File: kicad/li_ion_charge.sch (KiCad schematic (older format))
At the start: 1 part

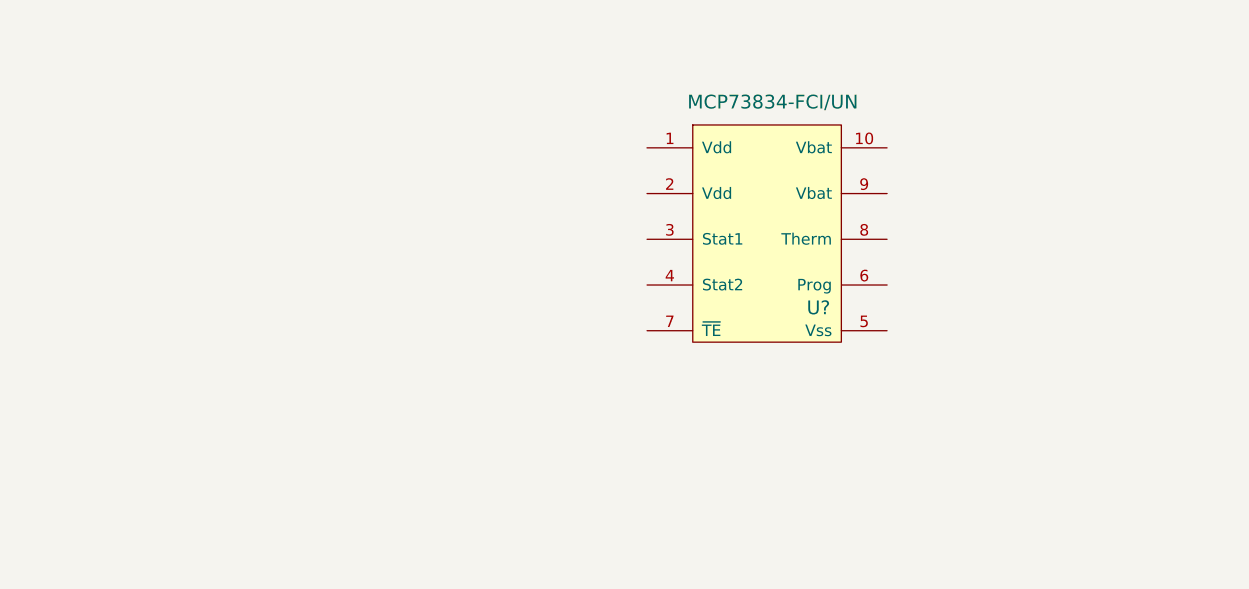
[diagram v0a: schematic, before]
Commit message: Initial implementation of schematic with values
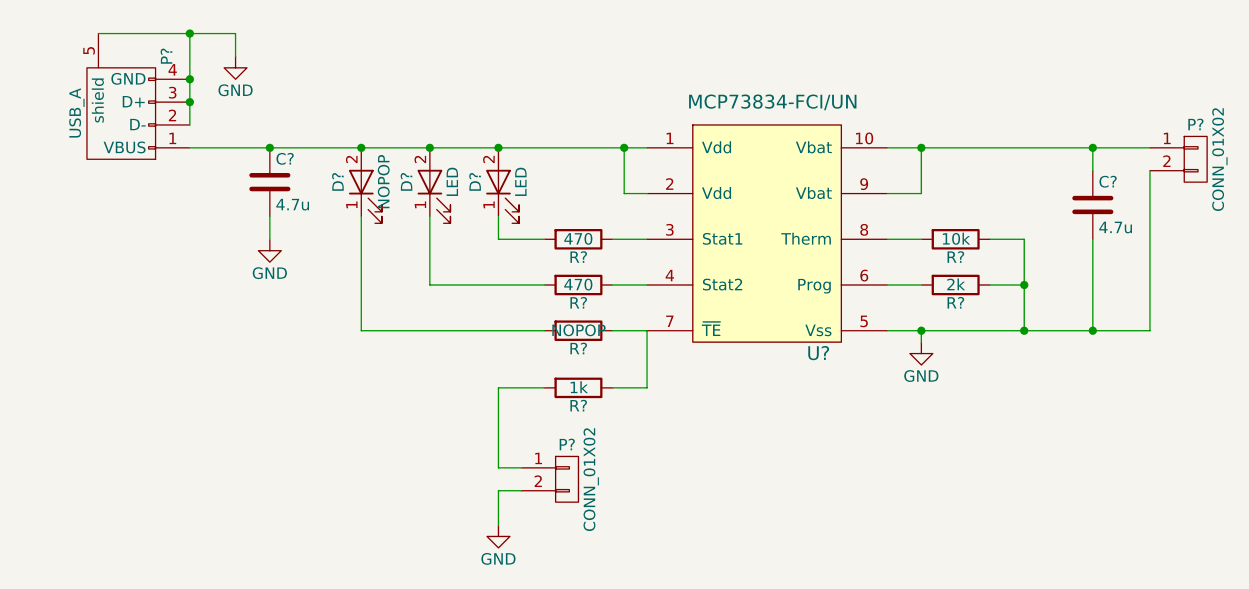
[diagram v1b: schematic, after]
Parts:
- removed U?: MCP73834-FCI/UN, symbol MCP73834-FCI/UN
- added C? (x2): 4.7u, symbol C
- added D? (x2): LED, symbol LED
- added D?: NOPOP, symbol LED
- added P? (x2): CONN_01X02, symbol CONN_01X02
- added P?: USB_A, symbol USB_A
- added R? (x2): 470, symbol R
- added R?: NOPOP, symbol R
- added R?: 2k, symbol R
- added R?: 10k, symbol R
- added R?: 1k, symbol R
- added U?: MCP73834-FCI/UN, symbol MCP73834-FCI/UN
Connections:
- new net: D?.1 (K), R?.2 (x3)
- new net: C?.1, D?.2 (A), D?.2 (A), D?.2 (A), P?.1 (VBUS), U?.1 (Vdd), U?.2 (Vdd)
- new net: R?.1, U?.4 (Stat2)
- new net: R?.1, R?.1, U?.7 (~TE)
- new net: R?.1, U?.3 (Stat1)
- new net: C?.1, P?.1 (P1), U?.10 (Vbat), U?.9 (Vbat)
- new net: R?.2, U?.6 (Prog)
- new net: R?.2, U?.8 (Therm)
- new net: P?.1 (P1), R?.2
- new net GND: C?.2, C?.2, P?.2 (D-), P?.2 (P2), P?.2 (P2), P?.3 (D+), P?.4 (GND), P?.5 (shield), R?.1, R?.1, U?.5 (Vss)

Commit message: Add footprint associations usinb CvPcb
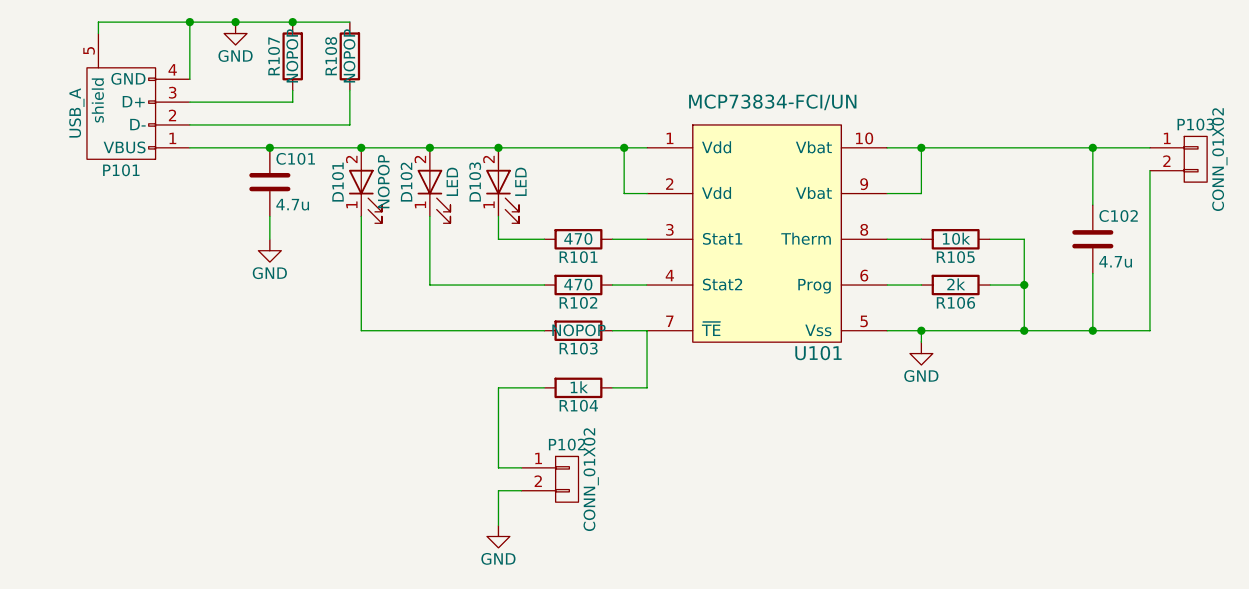
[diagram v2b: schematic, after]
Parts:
- added R107, R108: NOPOP, Resistors_SMD:R_0805_HandSoldering, symbol R
- C101, C102: renamed from C?; footprint (none) -> Capacitors_SMD:C_1206
- D101, D102, D103: renamed from D?; footprint (none) -> LEDs:LED_0805
- P101: renamed from P?; footprint (none) -> Connect:USB_A
- P102, P103: renamed from P?; footprint (none) -> Pin_Headers:Pin_Header_Angled_1x02_Pitch2.00mm
- R101, R102, R103, R104, R105, R106: renamed from R?; footprint (none) -> Resistors_SMD:R_0805_HandSoldering
- U101: renamed from U?; footprint (none) -> Housings_SSOP:MSOP-10_3x3mm_Pitch0.5mm
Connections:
- net GND: now also R107.2, R108.2; no longer P101.2 (D-), P101.3 (D+)
- new net: P101.2 (D-), R108.1
- new net: P101.3 (D+), R107.1
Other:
- moved on the sheet: C102
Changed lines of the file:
@@
 $EndDescr
 $Comp
-L LED D?
+L LED D103
 U 1 1 58BC7977
 P 4650 3500
-F 0 "D?" H 4650 3600 50  0000 C CNN
+F 0 "D103" H 4650 3600 50  0000 C CNN
 F 1 "LED" H 4650 3400 50  0000 C CNN
-F 2 "" H 4650 3500 50  0000 C CNN
+F 2 "LEDs:LED_0805" H 4650 3500 50  0001 C CNN
 F 3 "" H 4650 3500 50  0000 C CNN
 	1    4650 3500
@@
 $EndComp
 $Comp
-L LED D?
+L LED D101
 U 1 1 58BC79E4
 P 4050 3500
-F 0 "D?" H 4050 3600 50  0000 C CNN
+F 0 "D101" H 4050 3600 50  0000 C CNN
 F 1 "NOPOP" H 4050 3400 50  0000 C CNN
-F 2 "" H 4050 3500 50  0000 C CNN
+F 2 "LEDs:LED_0805" H 4050 3500 50  0001 C CNN
 F 3 "" H 4050 3500 50  0000 C CNN
 	1    4050 3500
@@
 $EndComp
 $Comp
-L LED D?
+L LED D102
 U 1 1 58BC7A05
 P 4350 3500
-F 0 "D?" H 4350 3600 50  0000 C CNN
+F 0 "D102" H 4350 3600 50  0000 C CNN
 F 1 "LED" H 4350 3400 50  0000 C CNN
-F 2 "" H 4350 3500 50  0000 C CNN
+F 2 "LEDs:LED_0805" H 4350 3500 50  0001 C CNN
 F 3 "" H 4350 3500 50  0000 C CNN
 	1    4350 3500
@@
 $EndComp
 $Comp
-L R R?
+L R R102
 U 1 1 58BC7A25
 P 5000 3950
-F 0 "R?" V 5080 3950 50  0000 C CNN
+F 0 "R102" V 5080 3950 50  0000 C CNN
 F 1 "470" V 5000 3950 50  0000 C CNN
-F 2 "" V 4930 3950 50  0000 C CNN
+F 2 "Resistors_SMD:R_0805_HandSoldering" V 4930 3950 50  0001 C CNN
 F 3 "" H 5000 3950 50  0000 C CNN
 	1    5000 3950
@@
 $EndComp
 $Comp
-L R R?
+L R R103
 U 1 1 58BC7BDA
 P 5000 4150
-F 0 "R?" V 5080 4150 50  0000 C CNN
+F 0 "R103" V 5080 4150 50  0000 C CNN
 F 1 "NOPOP" V 5000 4150 50  0000 C CNN
-F 2 "" V 4930 4150 50  0000 C CNN
+F 2 "Resistors_SMD:R_0805_HandSoldering" V 4930 4150 50  0001 C CNN
 F 3 "" H 5000 4150 50  0000 C CNN
 	1    5000 4150
@@
 $EndComp
 $Comp
-L R R?
+L R R101
 U 1 1 58BC7DA0
 P 5000 3750
-F 0 "R?" V 5080 3750 50  0000 C CNN
+F 0 "R101" V 5080 3750 50  0000 C CNN
 F 1 "470" V 5000 3750 50  0000 C CNN
-F 2 "" V 4930 3750 50  0000 C CNN
+F 2 "Resistors_SMD:R_0805_HandSoldering" V 4930 3750 50  0001 C CNN
 F 3 "" H 5000 3750 50  0000 C CNN
 	1    5000 3750
@@
 $EndComp
 $Comp
-L GND #PWR?
+L GND #PWR01
 U 1 1 58BC7FDA
 P 6500 4200
-F 0 "#PWR?" H 6500 3950 50  0001 C CNN
+F 0 "#PWR01" H 6500 3950 50  0001 C CNN
 F 1 "GND" H 6500 4050 50  0000 C CNN
 F 2 "" H 6500 4200 50  0000 C CNN
@@
 $EndComp
 $Comp
-L MCP73834-FCI/UN U?
+L MCP73834-FCI/UN U101
 U 1 1 58BC819D
 P 5800 3700
-F 0 "U?" H 6050 3150 60  0000 C CNN
+F 0 "U101" H 6050 3150 60  0000 C CNN
 F 1 "MCP73834-FCI/UN" H 5850 4250 60  0000 C CNN
-F 2 "" H 5800 3700 60  0001 C CNN
+F 2 "Housings_SSOP:MSOP-10_3x3mm_Pitch0.5mm" H 5800 3700 60  0001 C CNN
 F 3 "" H 5800 3700 60  0001 C CNN
 	1    5800 3700
@@
 $EndComp
 $Comp
-L R R?
+L R R106
 U 1 1 58BC8247
 P 6650 3950
-F 0 "R?" V 6730 3950 50  0000 C CNN
+F 0 "R106" V 6730 3950 50  0000 C CNN
 F 1 "2k" V 6650 3950 50  0000 C CNN
-F 2 "" V 6580 3950 50  0000 C CNN
+F 2 "Resistors_SMD:R_0805_HandSoldering" V 6580 3950 50  0001 C CNN
 F 3 "" H 6650 3950 50  0000 C CNN
 	1    6650 3950
@@
 $EndComp
 $Comp
-L R R?
+L R R105
 U 1 1 58BC82AB
 P 6650 3750
-F 0 "R?" V 6730 3750 50  0000 C CNN
+F 0 "R105" V 6730 3750 50  0000 C CNN
 F 1 "10k" V 6650 3750 50  0000 C CNN
-F 2 "" V 6580 3750 50  0000 C CNN
+F 2 "Resistors_SMD:R_0805_HandSoldering" V 6580 3750 50  0001 C CNN
 F 3 "" H 6650 3750 50  0000 C CNN
 	1    6650 3750
@@
 $EndComp
 $Comp
-L C C?
+L C C102
 U 1 1 58BC8729
-P 7250 3600
-F 0 "C?" H 7275 3700 50  0000 L CNN
-F 1 "4.7u" H 7275 3500 50  0000 L CNN
-F 2 "" H 7288 3450 50  0000 C CNN
-F 3 "" H 7250 3600 50  0000 C CNN
-	1    7250 3600
-	1    0    0    -1
-$EndComp
-$Comp
-L CONN_01X02 P?
+P 7250 3750
+F 0 "C102" H 7275 3850 50  0000 L CNN
+F 1 "4.7u" H 7275 3650 50  0000 L CNN
+F 2 "Capacitors_SMD:C_1206" H 7288 3600 50  0001 C CNN
+F 3 "" H 7250 3750 50  0000 C CNN
+	1    7250 3750
+	1    0    0    -1
+$EndComp
+$Comp
+L CONN_01X02 P103
 U 1 1 58BC886E
 P 7700 3400
-F 0 "P?" H 7700 3550 50  0000 C CNN
+F 0 "P103" H 7700 3550 50  0000 C CNN
 F 1 "CONN_01X02" V 7800 3400 50  0000 C CNN
-F 2 "" H 7700 3400 50  0000 C CNN
+F 2 "Pin_Headers:Pin_Header_Angled_1x02_Pitch2.00mm" H 7700 3400 50  0001 C CNN
 F 3 "" H 7700 3400 50  0000 C CNN
 	1    7700 3400
@@
 $EndComp
 $Comp
-L C C?
+L C C101
 U 1 1 58BC8A3D
 P 3650 3500
-F 0 "C?" H 3675 3600 50  0000 L CNN
+F 0 "C101" H 3675 3600 50  0000 L CNN
 F 1 "4.7u" H 3675 3400 50  0000 L CNN
-F 2 "" H 3688 3350 50  0000 C CNN
+F 2 "Capacitors_SMD:C_1206" H 3688 3350 50  0001 C CNN
 F 3 "" H 3650 3500 50  0000 C CNN
 	1    3650 3500
@@
 $EndComp
 $Comp
-L USB_A P?
+L USB_A P101
 U 1 1 58BC8AC7
 P 3000 3150
-F 0 "P?" H 3200 2950 50  0000 C CNN
+F 0 "P101" V 2700 3150 50  0000 C CNN
 F 1 "USB_A" H 2950 3350 50  0000 C CNN
-F 2 "" V 2950 3050 50  0000 C CNN
+F 2 "Connect:USB_A" V 2950 3050 50  0001 C CNN
 F 3 "" V 2950 3050 50  0000 C CNN
 	1    3000 3150
@@
 $EndComp
 $Comp
-L GND #PWR?
+L GND #PWR02
 U 1 1 58BC8BD8
 P 3650 3750
-F 0 "#PWR?" H 3650 3500 50  0001 C CNN
+F 0 "#PWR02" H 3650 3500 50  0001 C CNN
 F 1 "GND" H 3650 3600 50  0000 C CNN
 F 2 "" H 3650 3750 50  0000 C CNN
@@
 $EndComp
 $Comp
-L GND #PWR?
+L GND #PWR03
 U 1 1 58BC8EEB
-P 3500 2950
-F 0 "#PWR?" H 3500 2700 50  0001 C CNN
-F 1 "GND" H 3500 2800 50  0000 C CNN
-F 2 "" H 3500 2950 50  0000 C CNN
-F 3 "" H 3500 2950 50  0000 C CNN
-	1    3500 2950
-	1    0    0    -1
-$EndComp
-$Comp
-L R R?
+P 3500 2800
+F 0 "#PWR03" H 3500 2550 50  0001 C CNN
+F 1 "GND" H 3500 2650 50  0000 C CNN
+F 2 "" H 3500 2800 50  0000 C CNN
+F 3 "" H 3500 2800 50  0000 C CNN
+	1    3500 2800
+	1    0    0    -1
+$EndComp
+$Comp
+L R R104
 U 1 1 58BC907B
 P 5000 4400
-F 0 "R?" V 5080 4400 50  0000 C CNN
+F 0 "R104" V 5080 4400 50  0000 C CNN
 F 1 "1k" V 5000 4400 50  0000 C CNN
-F 2 "" V 4930 4400 50  0000 C CNN
+F 2 "Resistors_SMD:R_0805_HandSoldering" V 4930 4400 50  0001 C CNN
 F 3 "" H 5000 4400 50  0000 C CNN
 	1    5000 4400
@@
 $EndComp
 $Comp
-L CONN_01X02 P?
+L CONN_01X02 P102
 U 1 1 58BC9367
 P 4950 4800
-F 0 "P?" H 4950 4950 50  0000 C CNN
+F 0 "P102" H 4950 4950 50  0000 C CNN
 F 1 "CONN_01X02" V 5050 4800 50  0000 C CNN
-F 2 "" H 4950 4800 50  0000 C CNN
+F 2 "Pin_Headers:Pin_Header_Angled_1x02_Pitch2.00mm" H 4950 4800 50  0001 C CNN
 F 3 "" H 4950 4800 50  0000 C CNN
 	1    4950 4800
@@
 $EndComp
 $Comp
-L GND #PWR?
+L GND #PWR04
 U 1 1 58BC93FC
 P 4650 5000
-F 0 "#PWR?" H 4650 4750 50  0001 C CNN
+F 0 "#PWR04" H 4650 4750 50  0001 C CNN
 F 1 "GND" H 4650 4850 50  0000 C CNN
 F 2 "" H 4650 5000 50  0000 C CNN
@@
 Connection ~ 6500 3350
 Wire Wire Line
-	7250 3350 7250 3450
+	7250 3350 7250 3600
 Connection ~ 7250 3350
 Wire Wire Line
-	7250 4150 7250 3750
+	7250 4150 7250 3900
 Connection ~ 6950 4150
 Wire Wire Line
@@
 Connection ~ 3650 3350
 Wire Wire Line
-	2900 2850 3500 2850
-Wire Wire Line
-	3300 2850 3300 3250
-Connection ~ 3300 3150
-Connection ~ 3300 3050
-Wire Wire Line
-	3500 2850 3500 2950
-Connection ~ 3300 2850
-Wire Wire Line
 	4650 5000 4650 4850
 Wire Wire Line
@@
 Wire Wire Line
 	5300 4400 5300 4150
+$Comp
+L R R108
+U 1 1 58BC9A0D
+P 4000 2950
+F 0 "R108" V 4080 2950 50  0000 C CNN
+F 1 "NOPOP" V 4000 2950 50  0000 C CNN
+F 2 "Resistors_SMD:R_0805_HandSoldering" V 3930 2950 50  0001 C CNN
+F 3 "" H 4000 2950 50  0000 C CNN
+	1    4000 2950
+	-1   0    0    1
+$EndComp
+$Comp
+L R R107
+U 1 1 58BC9A97
+P 3750 2950
+F 0 "R107" V 3830 2950 50  0000 C CNN
+F 1 "NOPOP" V 3750 2950 50  0000 C CNN
+F 2 "Resistors_SMD:R_0805_HandSoldering" V 3680 2950 50  0001 C CNN
+F 3 "" H 3750 2950 50  0000 C CNN
+	1    3750 2950
+	-1   0    0    1
+$EndComp
+Wire Wire Line
+	3300 3250 4000 3250
+Wire Wire Line
+	4000 3250 4000 3100
+Wire Wire Line
+	3300 3150 3750 3150
+Wire Wire Line
+	3750 3150 3750 3100
+Wire Wire Line
+	2900 2850 2900 2800
+Wire Wire Line
+	2900 2800 4000 2800
+Connection ~ 3500 2800
+Connection ~ 3750 2800
+Wire Wire Line
+	3300 3050 3300 2800
+Connection ~ 3300 2800
 $EndSCHEMATC

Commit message: Minor update to schematic after adding initial layout
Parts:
- P102, P103: footprint Pin_Headers:Pin_Header_Angled_1x02_Pitch2.00mm -> Pin_Headers:Pin_Header_Straight_1x02_Pitch2.54mm
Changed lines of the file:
@@
 LIBS:valves
 LIBS:li_ion_charge
+LIBS:li_ion_charge-cache
 EELAYER 25 0
 EELAYER END
@@
 F 0 "P103" H 7700 3550 50  0000 C CNN
 F 1 "CONN_01X02" V 7800 3400 50  0000 C CNN
-F 2 "Pin_Headers:Pin_Header_Angled_1x02_Pitch2.00mm" H 7700 3400 50  0001 C CNN
+F 2 "Pin_Headers:Pin_Header_Straight_1x02_Pitch2.54mm" H 7700 3400 50  0001 C CNN
 F 3 "" H 7700 3400 50  0000 C CNN
 	1    7700 3400
@@
 F 0 "P102" H 4950 4950 50  0000 C CNN
 F 1 "CONN_01X02" V 5050 4800 50  0000 C CNN
-F 2 "Pin_Headers:Pin_Header_Angled_1x02_Pitch2.00mm" H 4950 4800 50  0001 C CNN
+F 2 "Pin_Headers:Pin_Header_Straight_1x02_Pitch2.54mm" H 4950 4800 50  0001 C CNN
 F 3 "" H 4950 4800 50  0000 C CNN
 	1    4950 4800

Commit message: Second iteration of the layout; added several net labels as well
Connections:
- net VIN: now reaches C101.1, D101.2 (A), D102.2 (A), D103.2 (A), P101.1 (VBUS), U101.1 (Vdd), U101.2 (Vdd)
- net Stat2: now reaches R102.1, U101.4 (Stat2)
- net ~TE: now reaches R103.1, R104.1, U101.7 (~TE)
- net Stat1: now reaches R101.1, U101.3 (Stat1)
- net VBAT: now reaches C102.1, P103.1 (P1), U101.10 (Vbat), U101.9 (Vbat)
- net Prog: now reaches R106.2, U101.6 (Prog)
- net Ther: now reaches R105.2, U101.8 (Therm)
- net RESET: now reaches P102.1 (P1), R104.2
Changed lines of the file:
@@
 	3300 3050 3300 2800
 Connection ~ 3300 2800
+Text Label 6850 3350 0    60   ~ 0
+VBAT
+Text Label 4700 3350 0    60   ~ 0
+VIN
+Text Label 4650 4700 1    60   ~ 0
+RESET
+Text Label 5300 4300 0    60   ~ 0
+~TE
+Text Label 6350 3750 0    60   ~ 0
+Ther
+Text Label 6350 3950 0    60   ~ 0
+Prog
+Text Label 5150 3750 0    60   ~ 0
+Stat1
+Text Label 5150 3950 0    60   ~ 0
+Stat2
 $EndSCHEMATC

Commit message: Add initial USB micro B footprint
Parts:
- P101: MPN (none) -> 10118193-0001LF
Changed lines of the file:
@@
 F 1 "USB_A" H 2950 3350 50  0000 C CNN
 F 2 "Connect:USB_A" V 2950 3050 50  0001 C CNN
-F 3 "" V 2950 3050 50  0000 C CNN
+F 3 "http://portal.fciconnect.com/Comergent//fci/drawing/10118193.pdf" V 2950 3050 50  0001 C CNN
+F 4 "10118193-0001LF" V 3000 3150 60  0001 C CNN "MPN"
 	1    3000 3150
 	0    -1   -1   0

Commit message: Add datasheet for USB to schematic
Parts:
- C101, C102: footprint Capacitors_SMD:C_1206 -> Capacitors_SMD:C_1206_HandSoldering
- P101: footprint Connect:USB_A -> li_ion_charge_library:USB_Micro-B
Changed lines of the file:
@@
 F 0 "C102" H 7275 3850 50  0000 L CNN
 F 1 "4.7u" H 7275 3650 50  0000 L CNN
-F 2 "Capacitors_SMD:C_1206" H 7288 3600 50  0001 C CNN
+F 2 "Capacitors_SMD:C_1206_HandSoldering" H 7288 3600 50  0001 C CNN
 F 3 "" H 7250 3750 50  0000 C CNN
 	1    7250 3750
@@
 F 0 "C101" H 3675 3600 50  0000 L CNN
 F 1 "4.7u" H 3675 3400 50  0000 L CNN
-F 2 "Capacitors_SMD:C_1206" H 3688 3350 50  0001 C CNN
+F 2 "Capacitors_SMD:C_1206_HandSoldering" H 3688 3350 50  0001 C CNN
 F 3 "" H 3650 3500 50  0000 C CNN
 	1    3650 3500
@@
 F 0 "P101" V 2700 3150 50  0000 C CNN
 F 1 "USB_A" H 2950 3350 50  0000 C CNN
-F 2 "Connect:USB_A" V 2950 3050 50  0001 C CNN
+F 2 "li_ion_charge_library:USB_Micro-B" V 2950 3050 50  0001 C CNN
 F 3 "http://portal.fciconnect.com/Comergent//fci/drawing/10118193.pdf" V 2950 3050 50  0001 C CNN
 F 4 "10118193-0001LF" V 3000 3150 60  0001 C CNN "MPN"

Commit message: change the schematic to use a micro USB part, and update netlist and layout accordingly
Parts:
- P101: value USB_A -> USB_B; symbol USB_A -> USB_OTG
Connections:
- net GND: now also P101.6 (Shield), R107.1, R108.1; no longer R107.2, R108.2
- net at P101.2 (D-): now also R107.2; no longer R108.1
- net at P101.3 (D+): now also R108.2; no longer R107.1
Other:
- moved on the sheet: R107, R108
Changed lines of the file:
@@
 EESchema Schematic File Version 2
+LIBS:li_ion_charge-rescue
 LIBS:power
 LIBS:device
@@
 $EndComp
 $Comp
-L USB_A P101
+L USB_OTG P101
 U 1 1 58BC8AC7
-P 3000 3150
-F 0 "P101" V 2700 3150 50  0000 C CNN
-F 1 "USB_A" H 2950 3350 50  0000 C CNN
-F 2 "li_ion_charge_library:USB_Micro-B" V 2950 3050 50  0001 C CNN
-F 3 "http://portal.fciconnect.com/Comergent//fci/drawing/10118193.pdf" V 2950 3050 50  0001 C CNN
-F 4 "10118193-0001LF" V 3000 3150 60  0001 C CNN "MPN"
-	1    3000 3150
-	0    -1   -1   0
+P 2850 3550
+F 0 "P101" V 2600 3550 50  0000 C CNN
+F 1 "USB_B" H 2850 3900 50  0000 C CNN
+F 2 "li_ion_charge_library:USB_Micro-B" V 2800 3450 50  0001 C CNN
+F 3 "http://portal.fciconnect.com/Comergent//fci/drawing/10118193.pdf" V 2800 3450 50  0001 C CNN
+F 4 "10118193-0001LF" V 2850 3550 60  0001 C CNN "MPN"
+	1    2850 3550
+	1    0    0    -1
 $EndComp
 $Comp
 L GND #PWR02
 U 1 1 58BC8BD8
-P 3650 3750
-F 0 "#PWR02" H 3650 3500 50  0001 C CNN
-F 1 "GND" H 3650 3600 50  0000 C CNN
-F 2 "" H 3650 3750 50  0000 C CNN
-F 3 "" H 3650 3750 50  0000 C CNN
-	1    3650 3750
-	1    0    0    -1
-$EndComp
-$Comp
-L GND #PWR03
-U 1 1 58BC8EEB
-P 3500 2800
-F 0 "#PWR03" H 3500 2550 50  0001 C CNN
-F 1 "GND" H 3500 2650 50  0000 C CNN
-F 2 "" H 3500 2800 50  0000 C CNN
-F 3 "" H 3500 2800 50  0000 C CNN
-	1    3500 2800
+P 3650 3700
+F 0 "#PWR02" H 3650 3450 50  0001 C CNN
+F 1 "GND" H 3650 3550 50  0000 C CNN
+F 2 "" H 3650 3700 50  0000 C CNN
+F 3 "" H 3650 3700 50  0000 C CNN
+	1    3650 3700
 	1    0    0    -1
 $EndComp
@@
 P 4950 4800
 F 0 "P102" H 4950 4950 50  0000 C CNN
-F 1 "CONN_01X02" V 5050 4800 50  0000 C CNN
+F 1 "CONN_01X02" H 4950 4650 50  0000 C CNN
 F 2 "Pin_Headers:Pin_Header_Straight_1x02_Pitch2.54mm" H 4950 4800 50  0001 C CNN
 F 3 "" H 4950 4800 50  0000 C CNN
@@
 $EndComp
 $Comp
-L GND #PWR04
+L GND #PWR03
 U 1 1 58BC93FC
 P 4650 5000
-F 0 "#PWR04" H 4650 4750 50  0001 C CNN
+F 0 "#PWR03" H 4650 4750 50  0001 C CNN
 F 1 "GND" H 4650 4850 50  0000 C CNN
 F 2 "" H 4650 5000 50  0000 C CNN
@@
 	5150 4150 5300 4150
 Wire Wire Line
-	3300 3350 5300 3350
+	3150 3350 5300 3350
 Wire Wire Line
 	5200 3350 5200 3550
@@
 Connection ~ 7250 4150
 Wire Wire Line
-	3650 3650 3650 3750
+	3650 3650 3650 3700
 Connection ~ 3650 3350
 Wire Wire Line
@@
 L R R108
 U 1 1 58BC9A0D
-P 4000 2950
-F 0 "R108" V 4080 2950 50  0000 C CNN
-F 1 "NOPOP" V 4000 2950 50  0000 C CNN
-F 2 "Resistors_SMD:R_0805_HandSoldering" V 3930 2950 50  0001 C CNN
-F 3 "" H 4000 2950 50  0000 C CNN
-	1    4000 2950
+P 3500 4050
+F 0 "R108" V 3580 4050 50  0000 C CNN
+F 1 "NOPOP" V 3500 4050 50  0000 C CNN
+F 2 "Resistors_SMD:R_0805_HandSoldering" V 3430 4050 50  0001 C CNN
+F 3 "" H 3500 4050 50  0000 C CNN
+	1    3500 4050
 	-1   0    0    1
 $EndComp
@@
 L R R107
 U 1 1 58BC9A97
-P 3750 2950
-F 0 "R107" V 3830 2950 50  0000 C CNN
-F 1 "NOPOP" V 3750 2950 50  0000 C CNN
-F 2 "Resistors_SMD:R_0805_HandSoldering" V 3680 2950 50  0001 C CNN
-F 3 "" H 3750 2950 50  0000 C CNN
-	1    3750 2950
+P 3300 4050
+F 0 "R107" V 3380 4050 50  0000 C CNN
+F 1 "NOPOP" V 3300 4050 50  0000 C CNN
+F 2 "Resistors_SMD:R_0805_HandSoldering" V 3230 4050 50  0001 C CNN
+F 3 "" H 3300 4050 50  0000 C CNN
+	1    3300 4050
 	-1   0    0    1
 $EndComp
-Wire Wire Line
-	3300 3250 4000 3250
-Wire Wire Line
-	4000 3250 4000 3100
-Wire Wire Line
-	3300 3150 3750 3150
-Wire Wire Line
-	3750 3150 3750 3100
-Wire Wire Line
-	2900 2850 2900 2800
-Wire Wire Line
-	2900 2800 4000 2800
-Connection ~ 3500 2800
-Connection ~ 3750 2800
-Wire Wire Line
-	3300 3050 3300 2800
-Connection ~ 3300 2800
 Text Label 6850 3350 0    60   ~ 0
 VBAT
@@
 Text Label 5150 3950 0    60   ~ 0
 Stat2
+Wire Wire Line
+	3150 3550 3500 3550
+Wire Wire Line
+	3500 3550 3500 3900
+Wire Wire Line
+	3150 3650 3300 3650
+Wire Wire Line
+	3300 3650 3300 3900
+Wire Wire Line
+	3150 4000 3150 3750
+Wire Wire Line
+	2750 4000 3150 4000
+Wire Wire Line
+	2750 3950 2750 4250
+Connection ~ 2750 4000
+Wire Wire Line
+	2850 3950 2850 4000
+Connection ~ 2850 4000
+$Comp
+L GND #PWR04
+U 1 1 58C427E6
+P 2750 4250
+F 0 "#PWR04" H 2750 4000 50  0001 C CNN
+F 1 "GND" H 2750 4100 50  0000 C CNN
+F 2 "" H 2750 4250 50  0000 C CNN
+F 3 "" H 2750 4250 50  0000 C CNN
+	1    2750 4250
+	1    0    0    -1
+$EndComp
+Wire Wire Line
+	3500 4200 3500 4250
+Wire Wire Line
+	3500 4250 2750 4250
+Wire Wire Line
+	3300 4200 3300 4250
+Connection ~ 3300 4250
 $EndSCHEMATC
